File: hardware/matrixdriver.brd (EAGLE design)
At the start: 51.7 x 61 mm, 46 parts, among them IC1 75176AD, IC2 4017D, IC3 ULN2803, IC4 7805T, J1 DCJ0202, Q1 CSM-7X-DU, Q2 MMBT4403LT1SMD, Q3 MMBT4403LT1SMD, Q4 MMBT4403LT1SMD, Q5 MMBT4403LT1SMD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

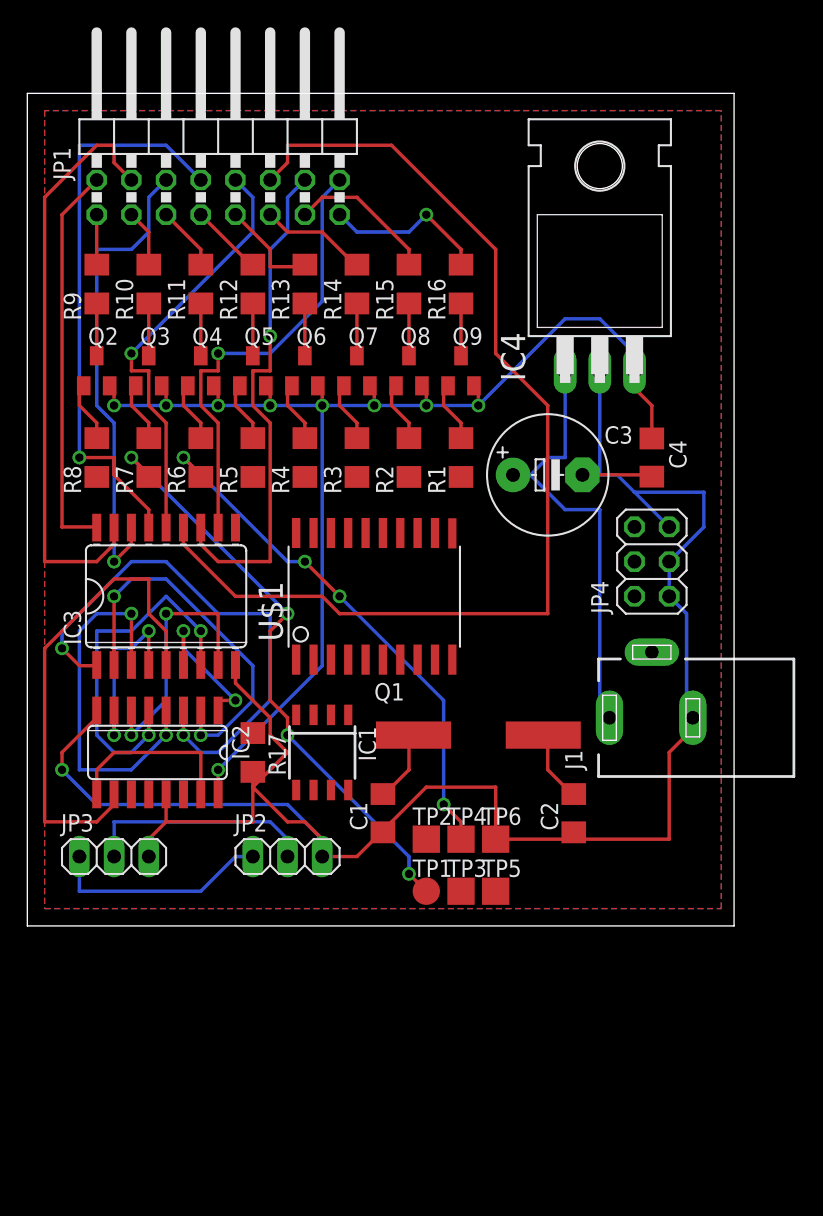
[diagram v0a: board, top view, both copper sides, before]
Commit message: Fully routed board
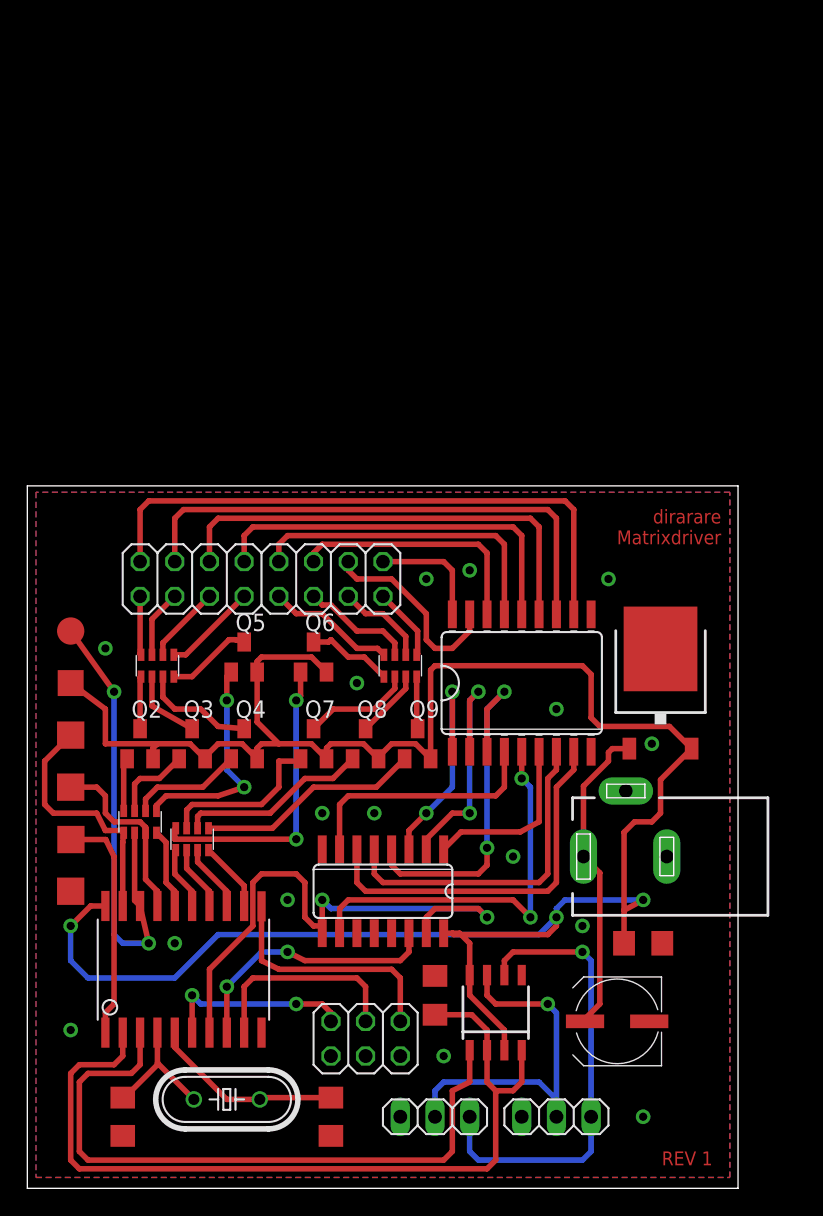
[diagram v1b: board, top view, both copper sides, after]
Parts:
- removed Q1: CSM-7X-DU, crystal:CSM-7X-DU
- removed R1, R2, R3, R4, R5, R6, R7, R8: 1k, resistor:R1206
- removed R10, R11, R12, R13, R14, R15, R16, R9: 10, resistor:R1206
- added CTS742C083_1, CTS742C083_2: 1k, resistor-net:CTS742C083
- added CTS742C083_3, CTS742C083_4: 10, resistor-net:CTS742C083
- added Q10: 20MHZ, adafruit:HC49/S
- C3: device rcl:E5-8,5 -> rcl:UD-6,3X5,8_NICHICON
- IC4: value 7805T -> 7805DT; device linear:TO220H -> linear:TO252
- JP1: device pinhead-fixdrills:2X08/90 -> pinhead-fixdrills:2X08
- JP4: value PORTSELECT -> P.SELECT
- TP2: value TPSQTP20SQ -> TPSQTP19SQ; device testpad:TP20SQ -> testpad:TP19SQ
- U$1: value TINY2313-*S* -> TINY2313
- moved JP4 40.7 mm to (24.8, 10.8), turned to 0 degrees
- moved C3 40.3 mm to (43.2, 12.1), turned to 180 degrees
- moved C4 35.6 mm to (45.1, 17.8), turned to 0 degrees
- moved IC4 33.3 mm to (46.4, 36.8)
- moved JP1 33.2 mm to (17.1, 44.5)
- moved TP1 32.3 mm to (3.17, 40.6), turned to 270 degrees
- moved TP6 31.3 mm to (3.17, 21.6), turned to 270 degrees
- moved TP5 31.3 mm to (3.19, 25.4), turned to 270 degrees
- moved TP3 30.8 mm to (3.17, 33.0), turned to 270 degrees
- moved U$1 30.7 mm to (11.4, 15.9)
- moved JP3 30.2 mm to (29.8, 5.08), turned to 180 degrees
- moved C1 29.3 mm to (6.99, 5.08)
- moved TP4 28.8 mm to (3.17, 29.2)
- moved C2 28.5 mm to (22.2, 5.08)
- moved TP2 28.4 mm to (3.17, 36.8), turned to 270 degrees
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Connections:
- removed net N$44: Q6.B, R4.2
- removed net N$45: Q5.B, R5.2
- removed net N$46: Q4.B, R6.2
- removed net N$47: Q3.B, R7.2
- removed net N$48: Q2.B, R8.2
- new net N$13: CTS742C083_4.8, JP1.9
- new net N$29: CTS742C083_4.7, JP1.11
- new net N$30: CTS742C083_4.6, JP1.13
- new net N$31: CTS742C083_4.5, JP1.15
- new net N$32: CTS742C083_1.7, Q3.B
- net GND: now also IC4.3; no longer IC4.2
- net N$1: now also CTS742C083_2.4; no longer R1.1
- net N$11: now also Q10.2; no longer Q1.1
- net N$12: now also Q10.1; no longer Q1.2
- net N$14: now also IC3.11; no longer IC3.18
- net N$2: now also CTS742C083_2.3; no longer R2.1
- net N$25: now also IC3.18; no longer IC3.11
- net N$26: now also IC3.17; no longer IC3.12
- net N$27: now also IC3.16; no longer IC3.13
- net N$28: now also IC3.15; no longer IC3.14
- net N$3: now also CTS742C083_2.2; no longer R3.1
- net N$33: now also CTS742C083_3.8; no longer R9.2
- net N$34: now also CTS742C083_3.7; no longer R10.2
- net N$35: now also CTS742C083_3.6; no longer R11.2
- net N$36: now also CTS742C083_3.5; no longer R12.2
- net N$37: now also CTS742C083_1.8, Q2.B; no longer JP1.9, R13.2
- net N$38: now also CTS742C083_1.6, Q4.B; no longer JP1.11, R14.2
- net N$39: now also CTS742C083_1.5, Q5.B; no longer JP1.13, R15.2
- net N$4: now also CTS742C083_2.1; no longer R4.1
- net N$40: now also CTS742C083_2.6, Q8.B; no longer JP1.15, R16.2
- net N$41: now also CTS742C083_2.5; no longer R1.2
- net N$42: now also CTS742C083_2.8, Q6.B; no longer Q8.B, R2.2
- net N$43: now also CTS742C083_2.7; no longer R3.2
- net N$49: now also CTS742C083_4.4; no longer R16.1
- net N$5: now also CTS742C083_1.4; no longer R5.1
- net N$50: now also CTS742C083_4.3; no longer R15.1
- net N$51: now also CTS742C083_4.2; no longer R14.1
- net N$52: now also CTS742C083_4.1; no longer R13.1
- net N$53: now also CTS742C083_3.4; no longer R12.1
- net N$54: now also CTS742C083_3.3; no longer R11.1
- net N$55: now also CTS742C083_3.2; no longer R10.1
- net N$56: now also CTS742C083_3.1; no longer R9.1
- net N$6: now also CTS742C083_1.3; no longer R6.1
- net N$63: now also IC3.12; no longer IC3.17
- net N$64: now also IC3.13; no longer IC3.16
- net N$66: now also IC3.14; no longer IC3.15
- net N$7: now also CTS742C083_1.2; no longer R7.1
- net N$8: now also CTS742C083_1.1; no longer R8.1
- net VCC: now also IC4.2, TP2.TP; no longer IC4.3
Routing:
- net GND: track 148.5 -> 0.00 mm, vias 1 -> 16
- net VCC: track 93.3 -> 167.6 mm, vias 9 -> 3
- net N$10: track 0.00 -> 62.6 mm
- net N$27: track 79.8 -> 18.4 mm
- net N$9: track 0.00 -> 48.4 mm
- net N$16: track 13.0 -> 41.9 mm, vias 0 -> 2
- net N$6: track 39.0 -> 13.6 mm, vias 4 -> 0
- net N$25: track 33.2 -> 8.57 mm, vias 1 -> 0
- net N$26: track 37.7 -> 14.8 mm, vias 1 -> 0
- net N$17: track 39.9 -> 17.2 mm
- net N$15: track 0.00 -> 19.5 mm, vias 0 -> 2
- net N$8: track 0.00 -> 18.1 mm
- net N$62: track 0.00 -> 17.7 mm
- net N$57: track 16.3 -> 33.9 mm, vias 0 -> 1
- net N$42: track 4.70 -> 22.1 mm, vias 0 -> 2
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- added copper zone on layer 1, net GND
- added copper zone on layer 16, net GND
- removed copper zone on layer 1, net N$13
- removed copper zone on layer 16, net N$29
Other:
- board size 51.7 x 61 mm -> 52 x 51.4 mm
- board text added: "REV 1"
- board text added: "dirarare Matrixdriver"
